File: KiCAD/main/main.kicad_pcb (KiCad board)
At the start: 2 copper layers, 61.5 x 60.5 mm, 20 parts, among them IC1 DHT22, J1 Sound Sensor, J2 BuckConverter, J3 Charge Controller, J4 Battery Status, J5 Anemometer, J6 Conn_02x04_Odd_Even, SW1 SW_SPDT, SW2 BOOT, SW3 RESET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

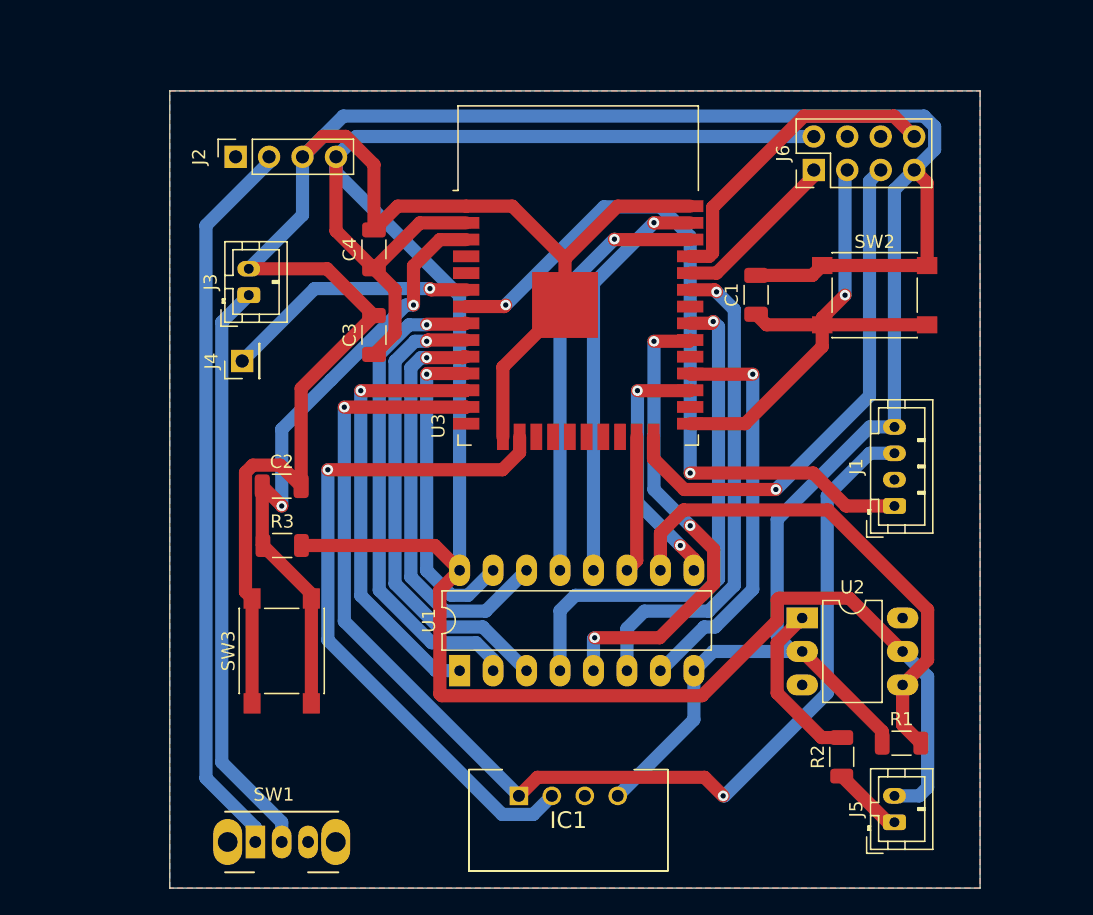
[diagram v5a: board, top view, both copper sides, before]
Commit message: Adjust tracks for 0.8mm width and 0.35mm clearance
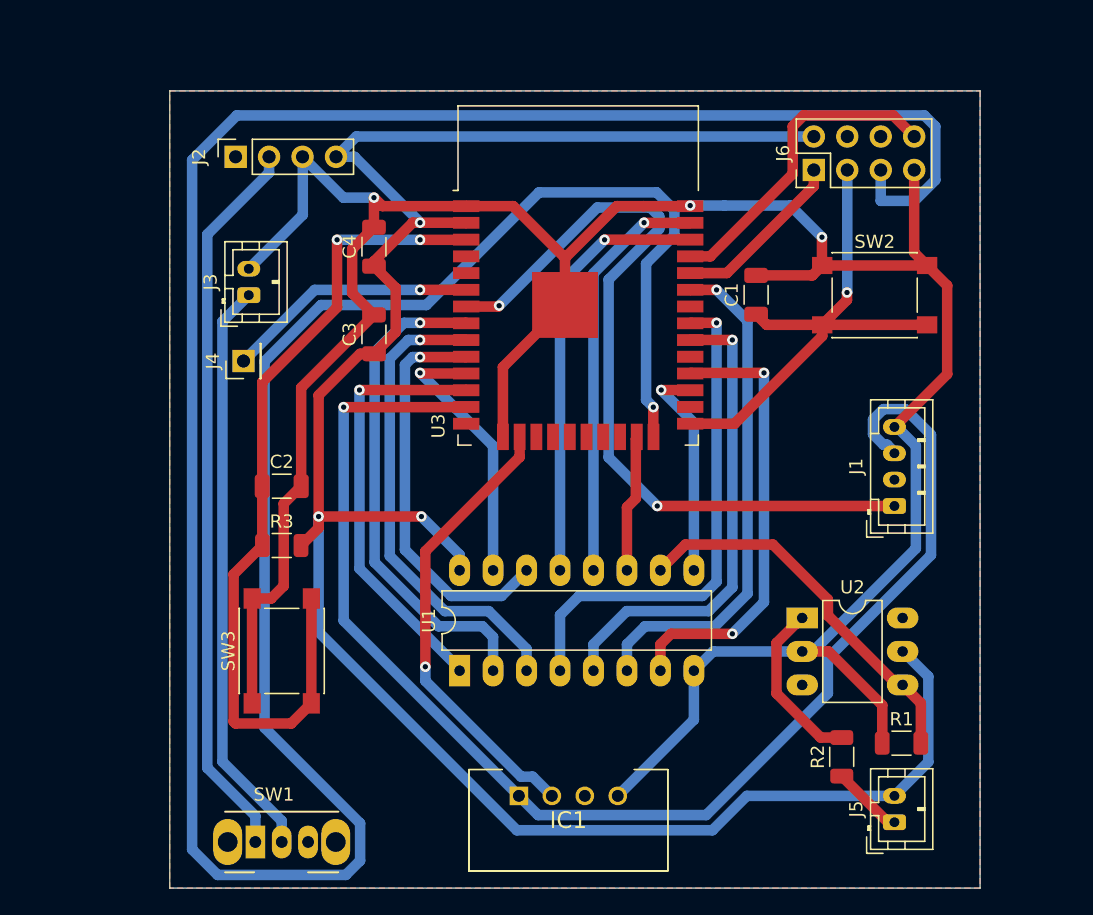
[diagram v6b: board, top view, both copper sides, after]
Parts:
- moved C4 0.20 mm to (116.5, 73.8)
- moved J4 0.10 mm to (106.6, 82.5)
- moved C3 0.05 mm to (116.5, 80.5)
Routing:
- net /Microcontroller/IO2: track 39.5 -> 231.9 mm
- net GND: track 262.5 -> 206.3 mm, vias 0 -> 3
- net /DHT22_Data: track 52.3 -> 34.7 mm
- net /Microcontroller/EN: track 47.7 -> 64.2 mm
- net /supply_on: track 93.5 -> 104.0 mm, vias 2 -> 1
- net +3V3: track 175.6 -> 165.1 mm, vias 0 -> 3
- net /Opto_Anemometer_Out: track 38.4 -> 29.3 mm
- net /Sound_Signal: track 55.5 -> 61.1 mm
- net /Microcontroller/IO26: track 24.5 -> 20.8 mm
- net /Microcontroller/IO17: track 30.7 -> 34.2 mm, vias 1 -> 2
- net /Microcontroller/IO16: track 19.4 -> 16.9 mm, vias 2 -> 1
- net /Microcontroller/I021: track 37.6 -> 38.8 mm
- net /Microcontroller/IO25: track 31.6 -> 30.5 mm
- net /Microcontroller/IO27: track 33.4 -> 32.6 mm
- net /Microcontroller/IO33: track 35.7 -> 36.3 mm
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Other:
- net class Default: clearance 0.2 -> 0.35; trace_width 1 -> 0.8; via_dia 1.2 -> 0.8; via_drill 0.8 -> 0.4
- rule trace_clearance: 0.2 -> 0.35

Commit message: Extend PCB limits and add M3 mounting holes
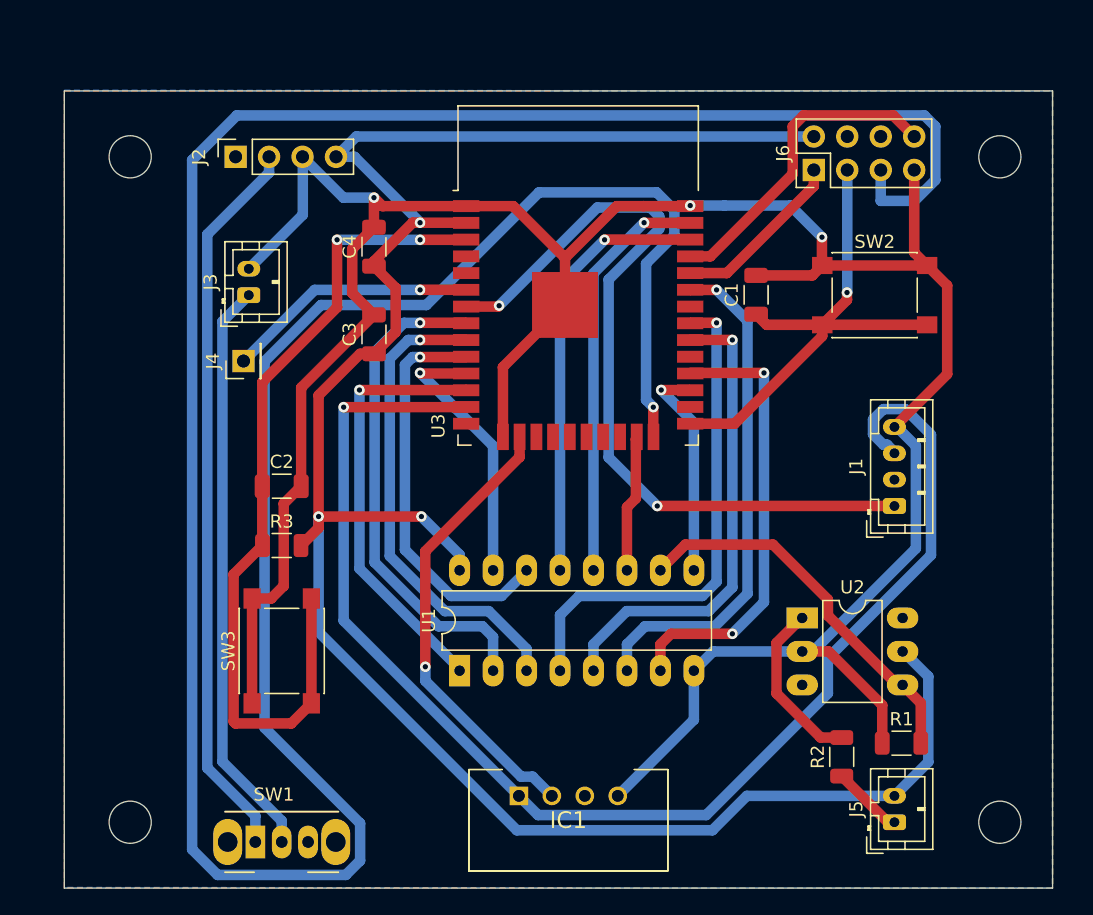
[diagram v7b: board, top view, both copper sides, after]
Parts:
- added REF**: MountingHole_3.2mm_M3, MountingHole:MountingHole_3.2mm_M3, F.Cu at (164.0, 117.5)
- added REF**: MountingHole_3.2mm_M3, MountingHole:MountingHole_3.2mm_M3, F.Cu at (164.0, 67.0)
- added REF**: MountingHole_3.2mm_M3, MountingHole:MountingHole_3.2mm_M3, F.Cu at (98.0, 117.5)
- added REF**: MountingHole_3.2mm_M3, MountingHole:MountingHole_3.2mm_M3, F.Cu at (98.0, 67.0)
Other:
- board size 61.5 x 60.5 mm -> 75 x 60.5 mm

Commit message: Fix pcb width
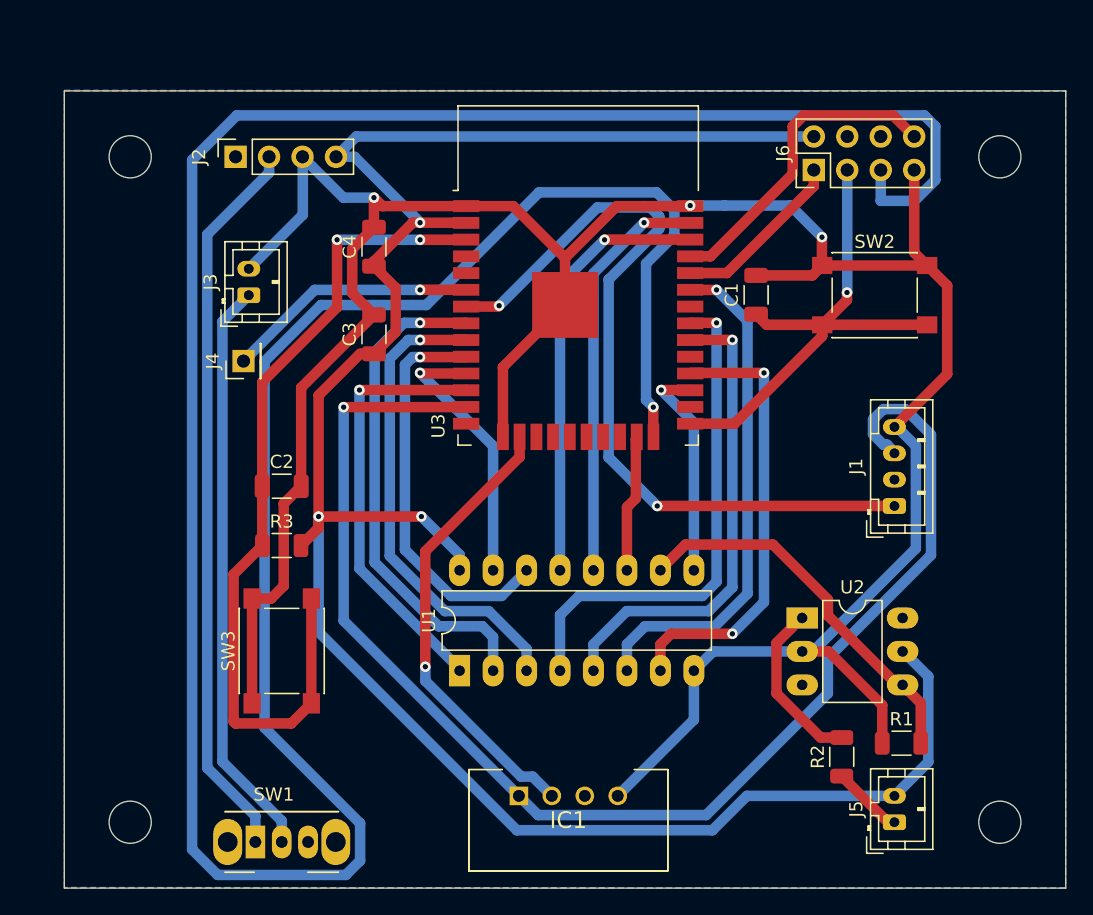
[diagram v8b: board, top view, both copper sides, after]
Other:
- board size 75 x 60.5 mm -> 76 x 60.5 mm
